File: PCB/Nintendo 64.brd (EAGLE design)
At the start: 58.5 x 61 mm, 13 parts

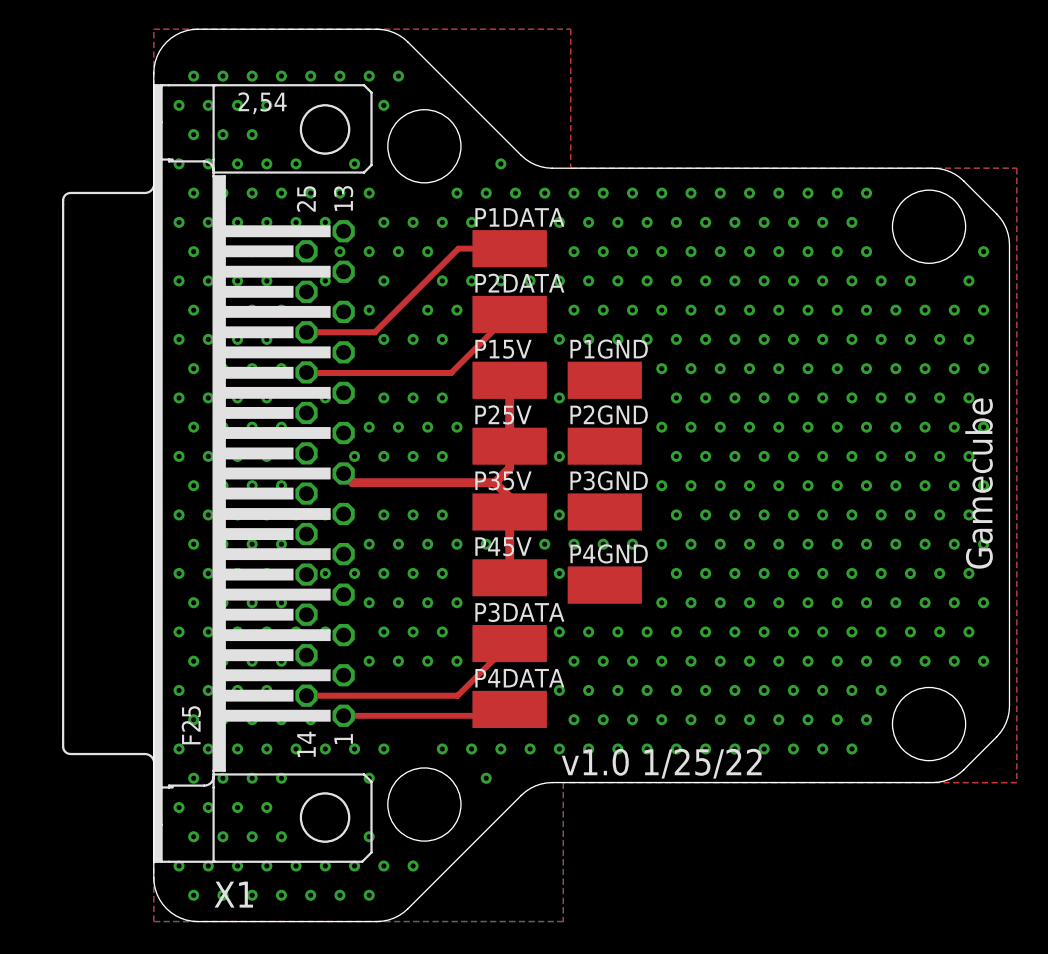
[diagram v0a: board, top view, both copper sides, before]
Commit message: PCB Updates/New Additions
All existing PCBs had silkscreen updates and NES, Virtual Boy, PSX/PS2, Nintendo 64, Saturn have been added.
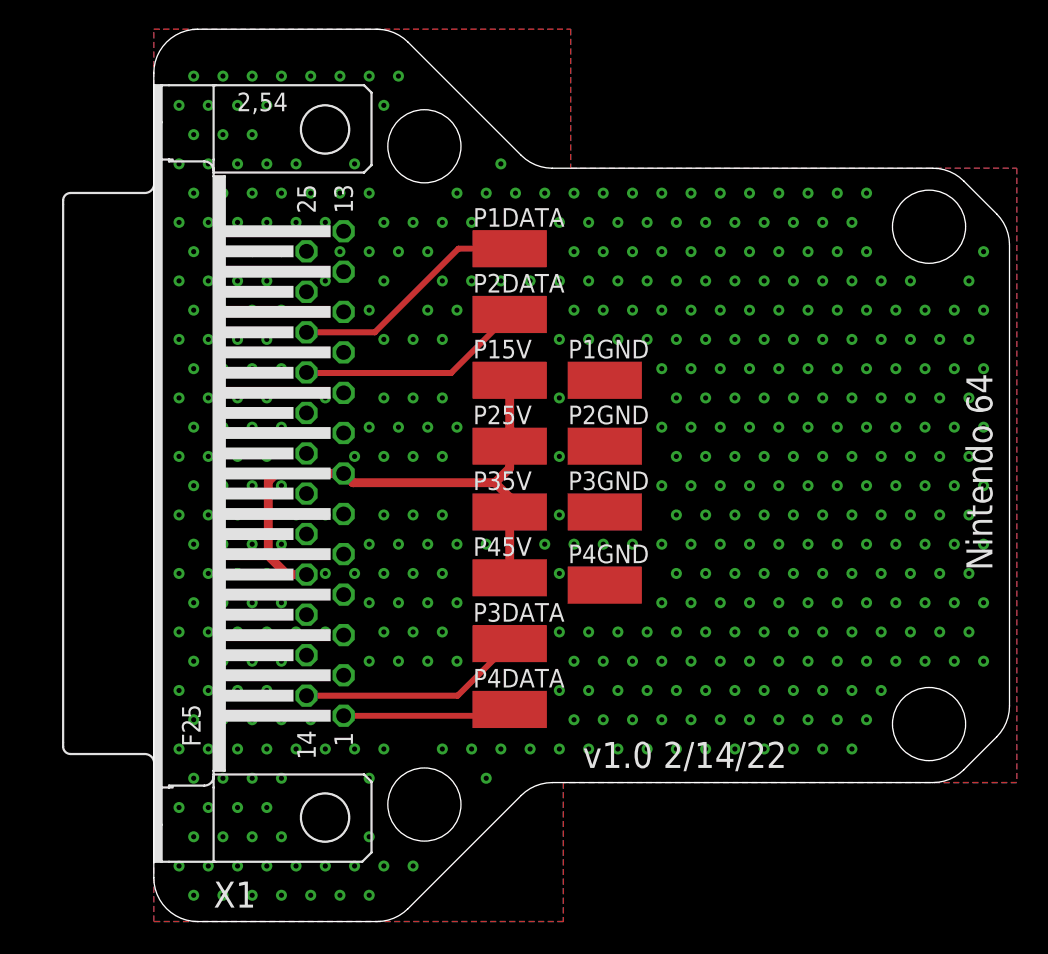
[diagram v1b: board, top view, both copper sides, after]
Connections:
- removed net 5VIN: P15V.1, P25V.1, P35V.1, P45V.1, X1.7
- new net 3V3IN: P15V.1, P25V.1, P35V.1, P45V.1, X1.17, X1.7
- net GND: no longer X1.17
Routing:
- net 3V3IN: track 0.00 -> 38.5 mm
- net 5VIN: track 24.9 -> 0.00 mm
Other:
- board text added: "Nintendo 64"
- board text added: "v1.0 2/14/22"
- board text removed: "Gamecube"
- board text removed: "v1.0 1/25/22"

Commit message: Datasheets, BOM Update, 3 New PCBs
Added Datasheets for the Female/Male DB25 connectors
Updated formatting on the BOM

New PCBs:
Added Nintendo 64 (Updated to 1.1, Moved VIN from 5V to 3V3)
Added Sega Saturn (Updated to 1.1, Added 5V and GND Pads on bottom for Second player pads to ease install)
Added NES

Removed PSX/PS2 and Virtual Boy as work is not complete (New branches will be made for each one)
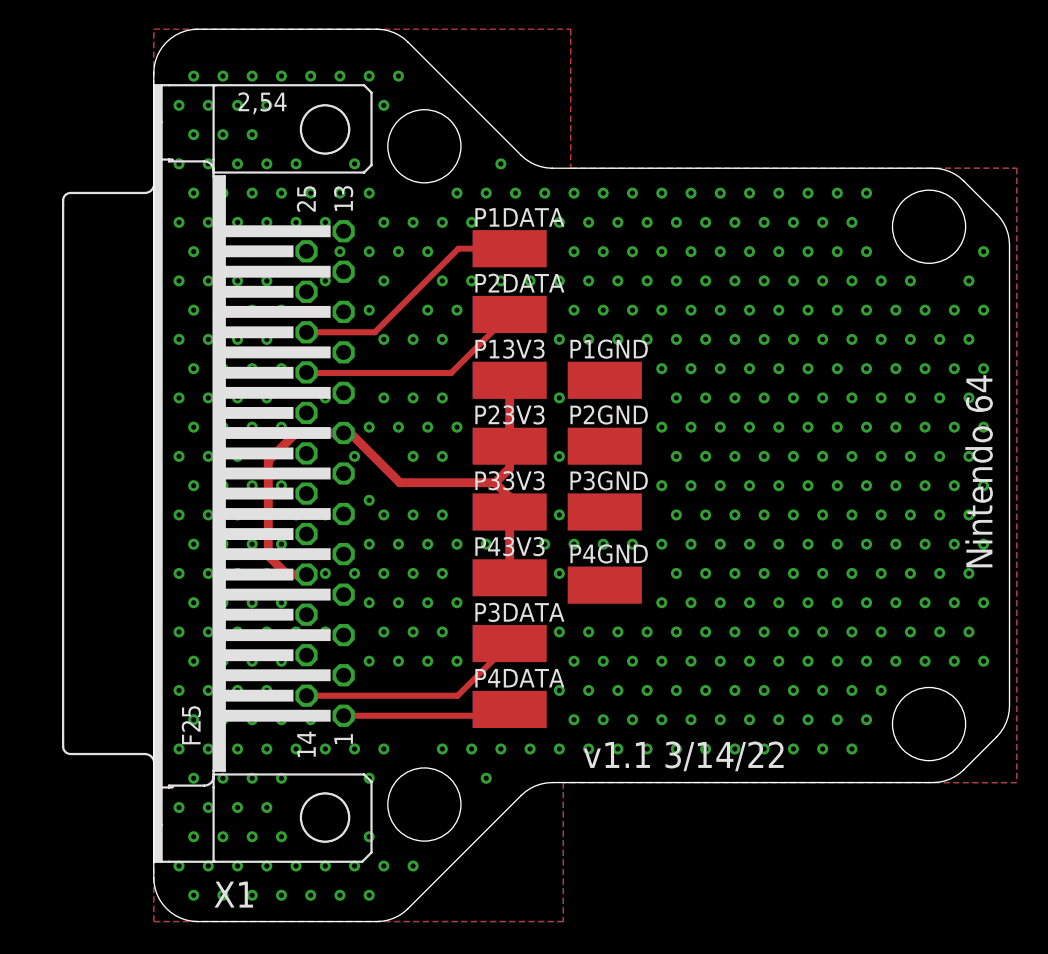
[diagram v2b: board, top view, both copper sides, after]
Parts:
- renumbered P15V to P13V3, P25V to P23V3, P35V to P33V3, P45V to P43V3
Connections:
- net 3V3IN: now also X1.8; no longer X1.7
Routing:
- net 3V3IN: track 38.5 -> 41.7 mm
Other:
- board text added: "v1.1 3/14/22"
- board text removed: "v1.0 2/14/22"

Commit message: PCB Update for better Housing Fit
All the PCBs were updated for better housing fitment.

Common Changes across all PCBs:
1. All Aux PCBs are now the exact same size.  (there was a .1mm-.5mm Variance previous)
2. All Aux PCBs Mounting holes are in the same location (there was a .05mm-.1mm Variance previous)
3. The DB25 has been moved 1.2mm close to the edge of the PCB for better connection when in the housing.

PCB Specific Updates:
3DO - Rename Pads (Removed trailing numbers), Flipped U2 to match U1, Moved U1 & U2 to same coordinates as other 2 Component PCBs in collection.

PCE & NES- Moved U1 & U2 to same coordinates as other 2 Component PCBs in collection.

PS2/PSX & Saturn - Added Notch on back edge of PCB for access for wires that need to attach to bottom layer of PCB.

All Gerbers have been updated.

New PCBs have been ordered for testing.
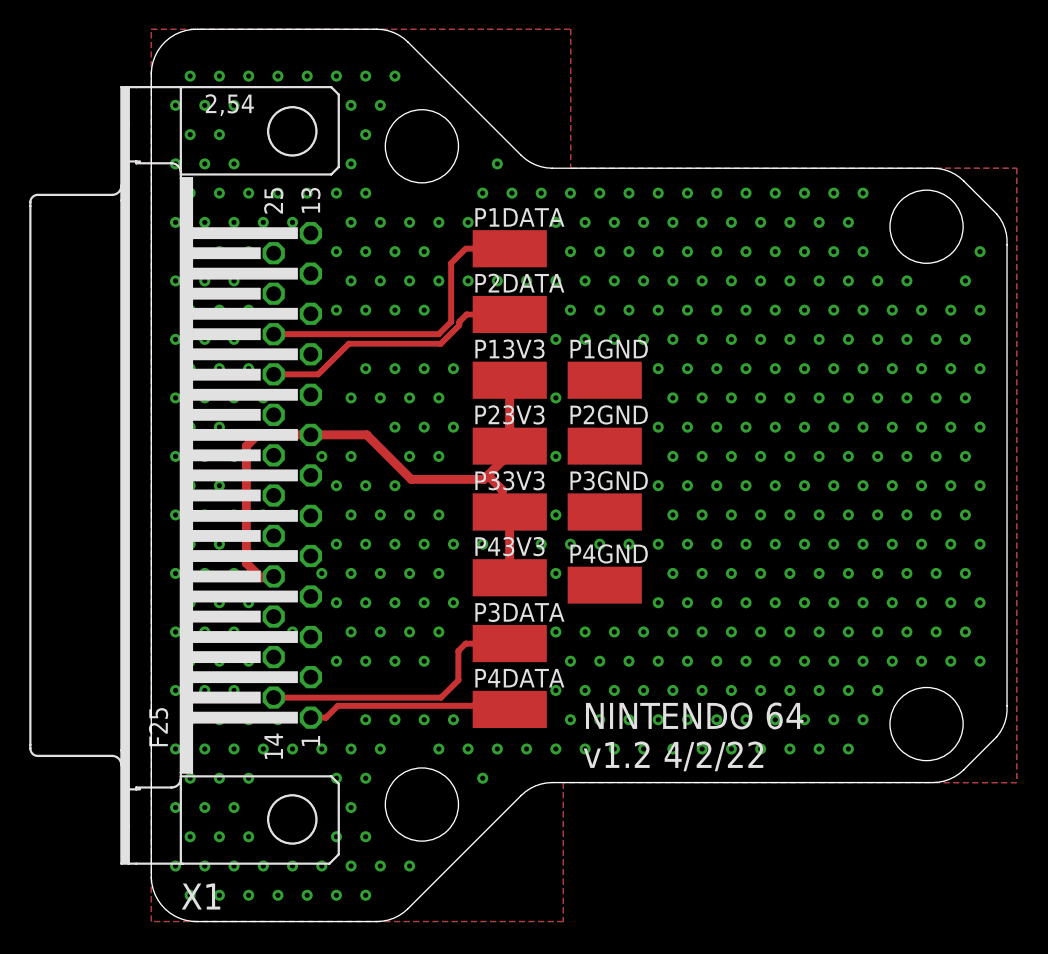
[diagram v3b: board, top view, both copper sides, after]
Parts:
- moved X1 2.24 mm to (9.64, 30.5)
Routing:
- net IO19: track 16.3 -> 20.9 mm
- net IO26: track 15.4 -> 18.8 mm
- net IO27: track 11.5 -> 14.0 mm
- net IO5: track 15.6 -> 18.0 mm
- net 3V3IN: track 41.7 -> 44.0 mm
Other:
- outline, holes or cut-outs redrawn
- board text added: "NINTENDO 64 v1.2 4/2/22"
- board text removed: "Nintendo 64"
- board text removed: "v1.1 3/14/22"

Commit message: Changed Player Order for N64 and Gamecube
Reversed the player order of the pads on the PCB, when installing in the housing the controller wires would twist.  this resolves that issue.
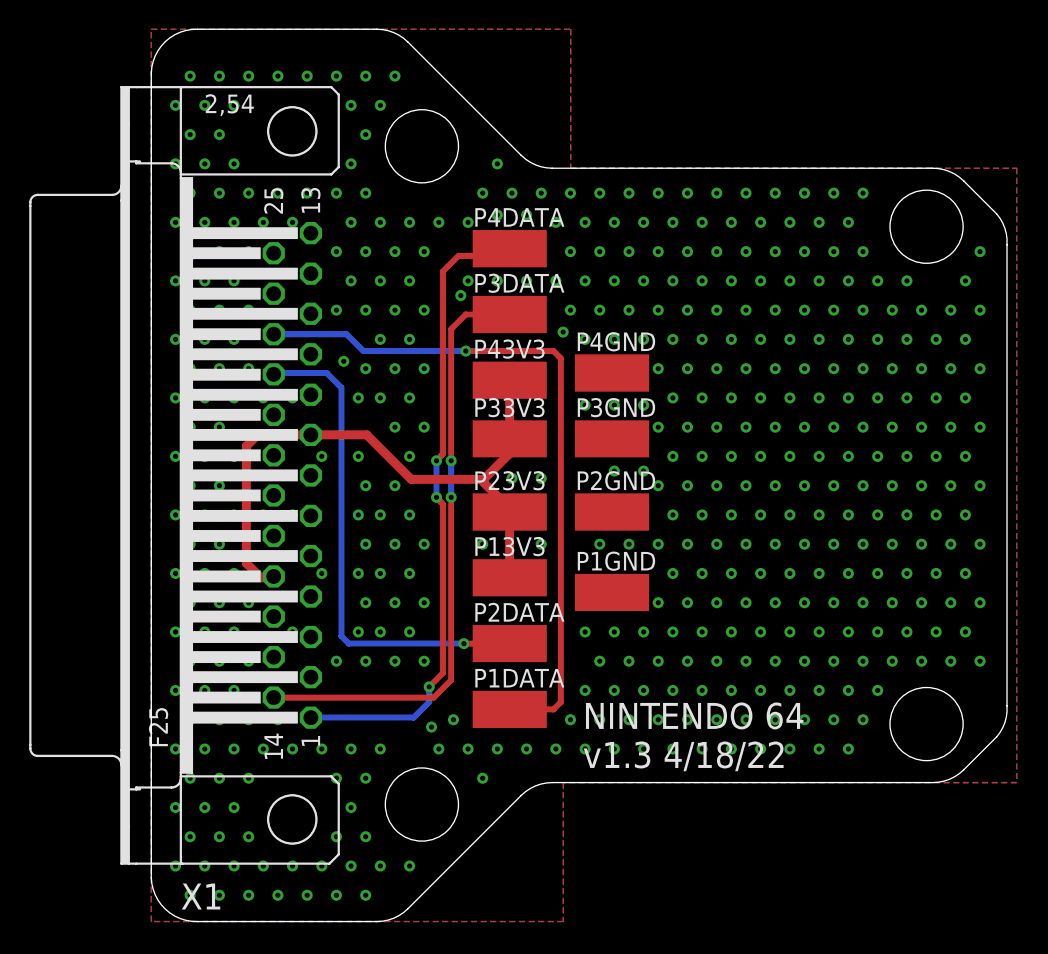
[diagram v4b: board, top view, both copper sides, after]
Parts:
- moved P1DATA 31.5 mm to (24.5, 14.5)
- moved P4DATA 31.5 mm to (24.5, 46.0)
- moved P2DATA 22.5 mm to (24.5, 19.0)
- moved P3DATA 22.5 mm to (24.5, 41.5)
- moved P1GND 14.5 mm to (31.5, 22.5)
- moved P4GND 14.5 mm to (31.5, 37.5)
- moved P13V3 13.5 mm to (24.5, 23.5)
- moved P43V3 13.5 mm to (24.5, 37.0)
- moved P3GND 5.02 mm to (31.5, 33.0)
- moved P33V3 5.00 mm to (24.5, 33.0)
- moved P2GND 4.53 mm to (31.5, 28.0)
- moved P23V3 4.50 mm to (24.5, 28.0)
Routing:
- net IO27: track 14.0 -> 43.9 mm, vias 0 -> 3
- net IO19: track 20.9 -> 47.5 mm, vias 0 -> 1
- net IO26: track 18.8 -> 41.0 mm, vias 0 -> 2
- net IO5: track 18.0 -> 33.8 mm, vias 0 -> 1
- net 3V3IN: track 44.0 -> 43.2 mm
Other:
- board text added: "NINTENDO 64 v1.3 4/18/22"
- board text removed: "NINTENDO 64 v1.2 4/2/22"

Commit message: Added exposed GND plane at DB25 anchors
All PCBs have been update to have exposed GND plane pads for the DB25 anchor points.

This resolves Issue 54
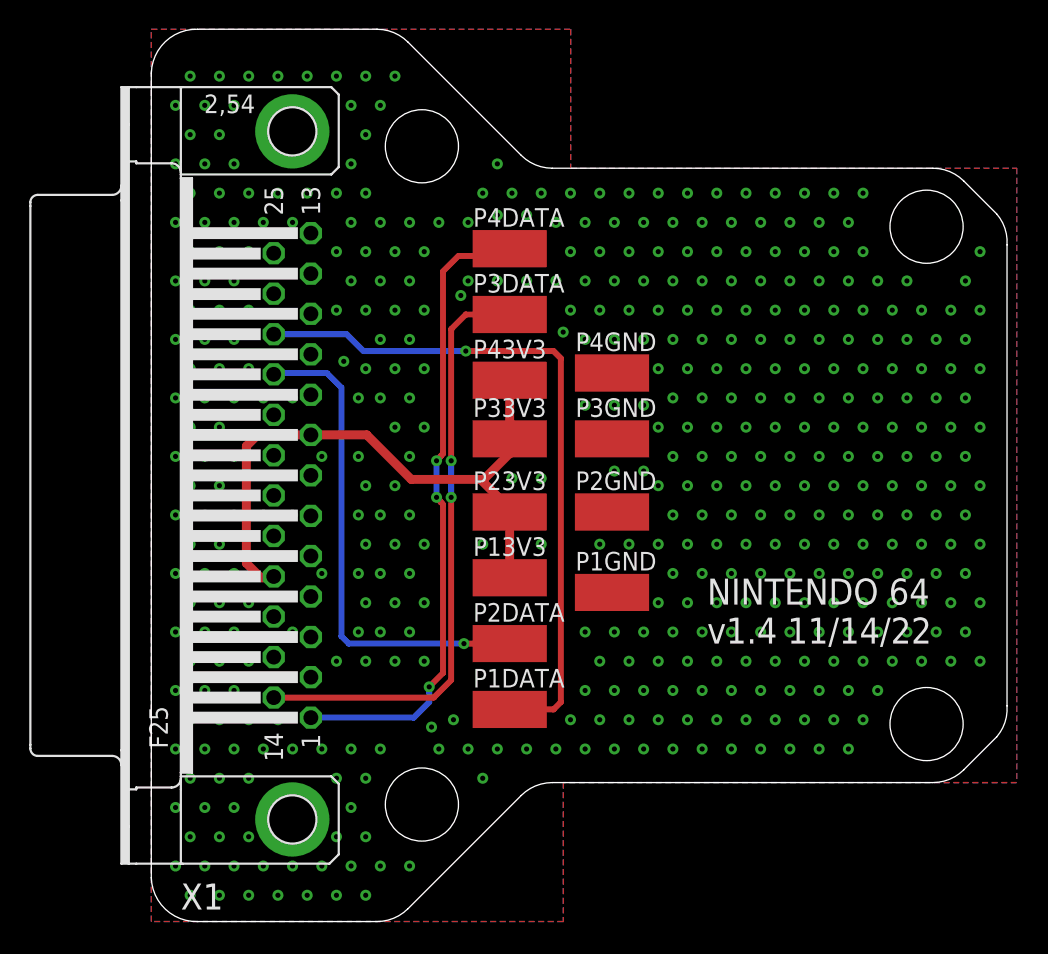
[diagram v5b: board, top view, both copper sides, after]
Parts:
- X1: device SparkFun-Retired:F25H -> SparkFun-Retired:F25HP
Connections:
- net GND: now also X1.GND1, X1.GND2
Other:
- board text added: "NINTENDO 64 v1.4 11/14/22"
- board text removed: "NINTENDO 64 v1.3 4/18/22"
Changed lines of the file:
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@@
 <hole x="18.5" y="53" drill="5"/>
 <hole x="18.5" y="8" drill="5"/>
-<text x="29.5" y="10.5" size="1.778" layer="21">NINTENDO 64
-v1.3 4/18/22</text>
+<text x="38" y="19" size="1.778" layer="21">NINTENDO 64
+v1.4 11/14/22</text>
 </plain>
 <attributes>
@@
 <attribute name="VALUE" x="31.5" y="37.5" size="0.0254" layer="27" rot="R270"/>
 </element>
-<element name="X1" library="SparkFun-Retired" package="F25H" value="" x="9.64" y="30.5" smashed="yes" rot="R90">
+<element name="X1" library="SparkFun-Retired" package="F25HP" value="" x="9.64" y="30.5" smashed="yes" rot="R90">
 <attribute name="NAME" x="4.919" y="2.6" size="1.778" layer="25" ratio="10" rot="R180"/>
 <attribute name="VALUE" x="-4.33" y="22.118" size="1.778" layer="27" ratio="10" rot="R90"/>
@@
 <via x="55.6568" y="43.7968" extent="1-16" drill="0.35"/>
 <via x="56.6568" y="45.7968" extent="1-16" drill="0.35"/>
+<contactref element="X1" pad="GND1"/>
+<contactref element="X1" pad="GND2"/>
 </signal>
 <signal name="IO5">
